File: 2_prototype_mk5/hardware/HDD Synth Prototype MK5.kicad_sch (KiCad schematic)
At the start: 11 parts, among them U2 Optocoupler_DC_PhotoNPN_AKEC

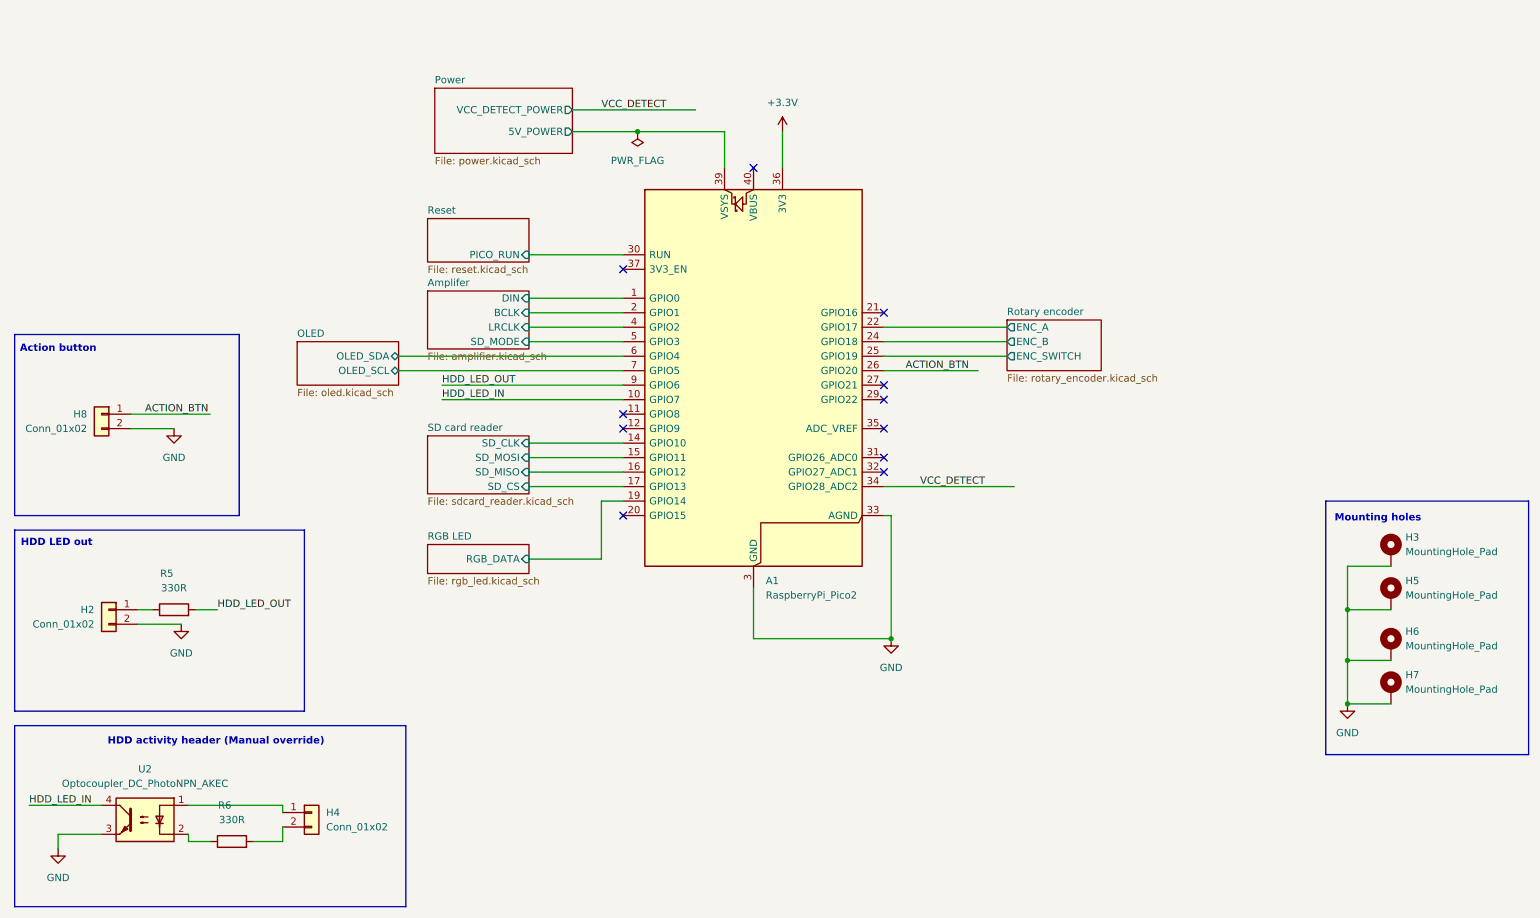
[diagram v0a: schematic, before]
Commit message: MKV - SATA connector and wiring complete
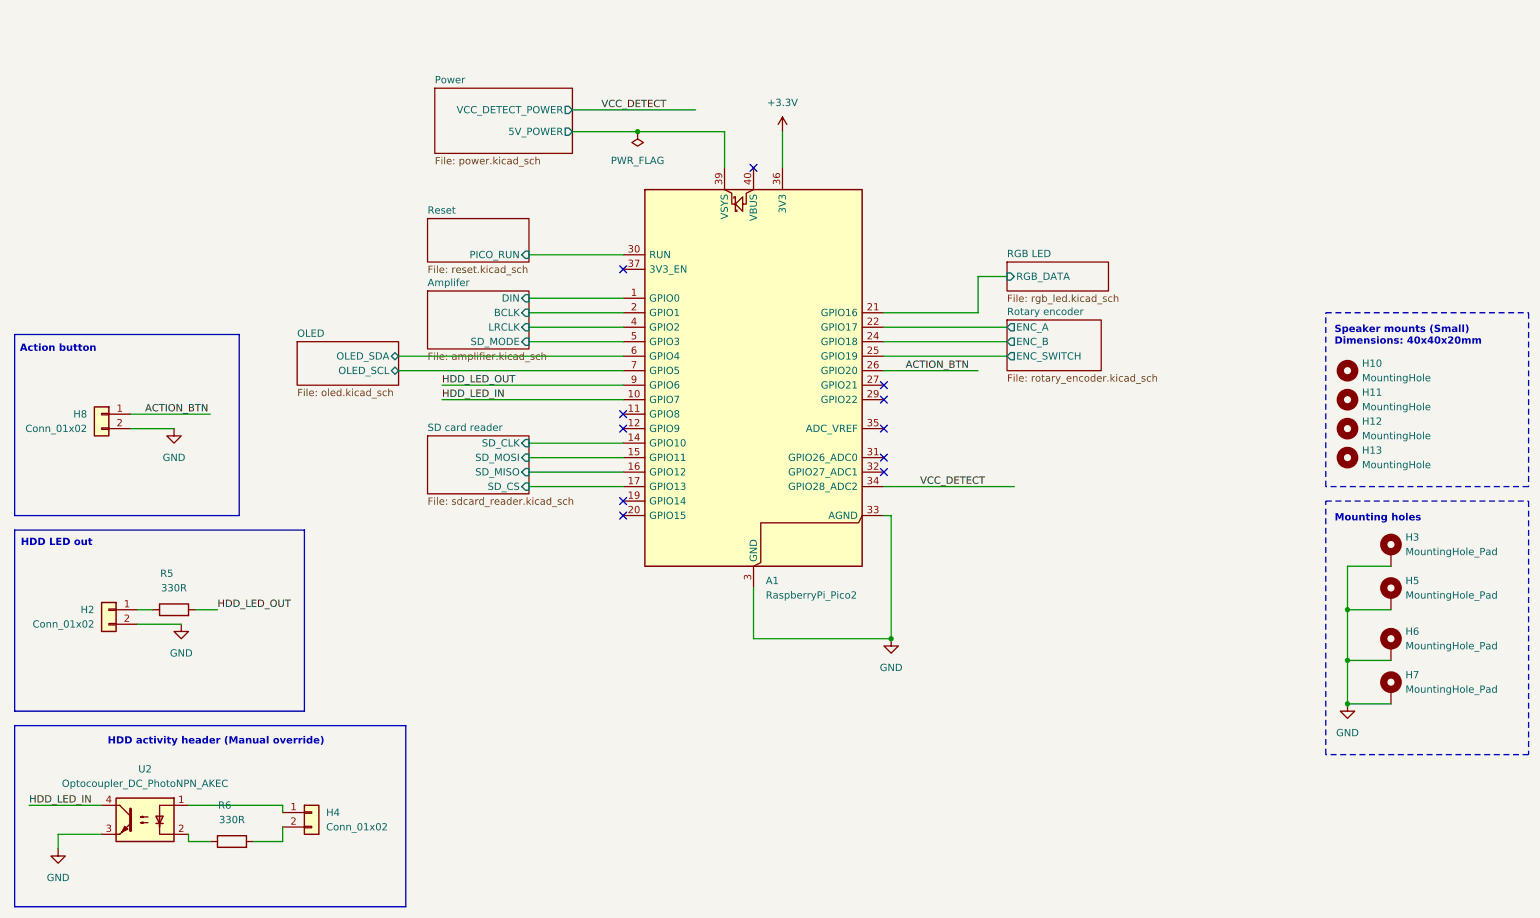
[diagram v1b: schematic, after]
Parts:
- added H10, H11, H12, H13: MountingHole, MountingHole:MountingHole_3.2mm_M3, symbol Mechanical:MountingHole
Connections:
- net RGB LED/RGB_DATA: now also A1.21 (GPIO16); no longer A1.19 (GPIO14)
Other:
- note added: "Speaker mounts (Small) Dimensions: 40x40x20mm"

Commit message: Major MKV redesign using embedded RP2350
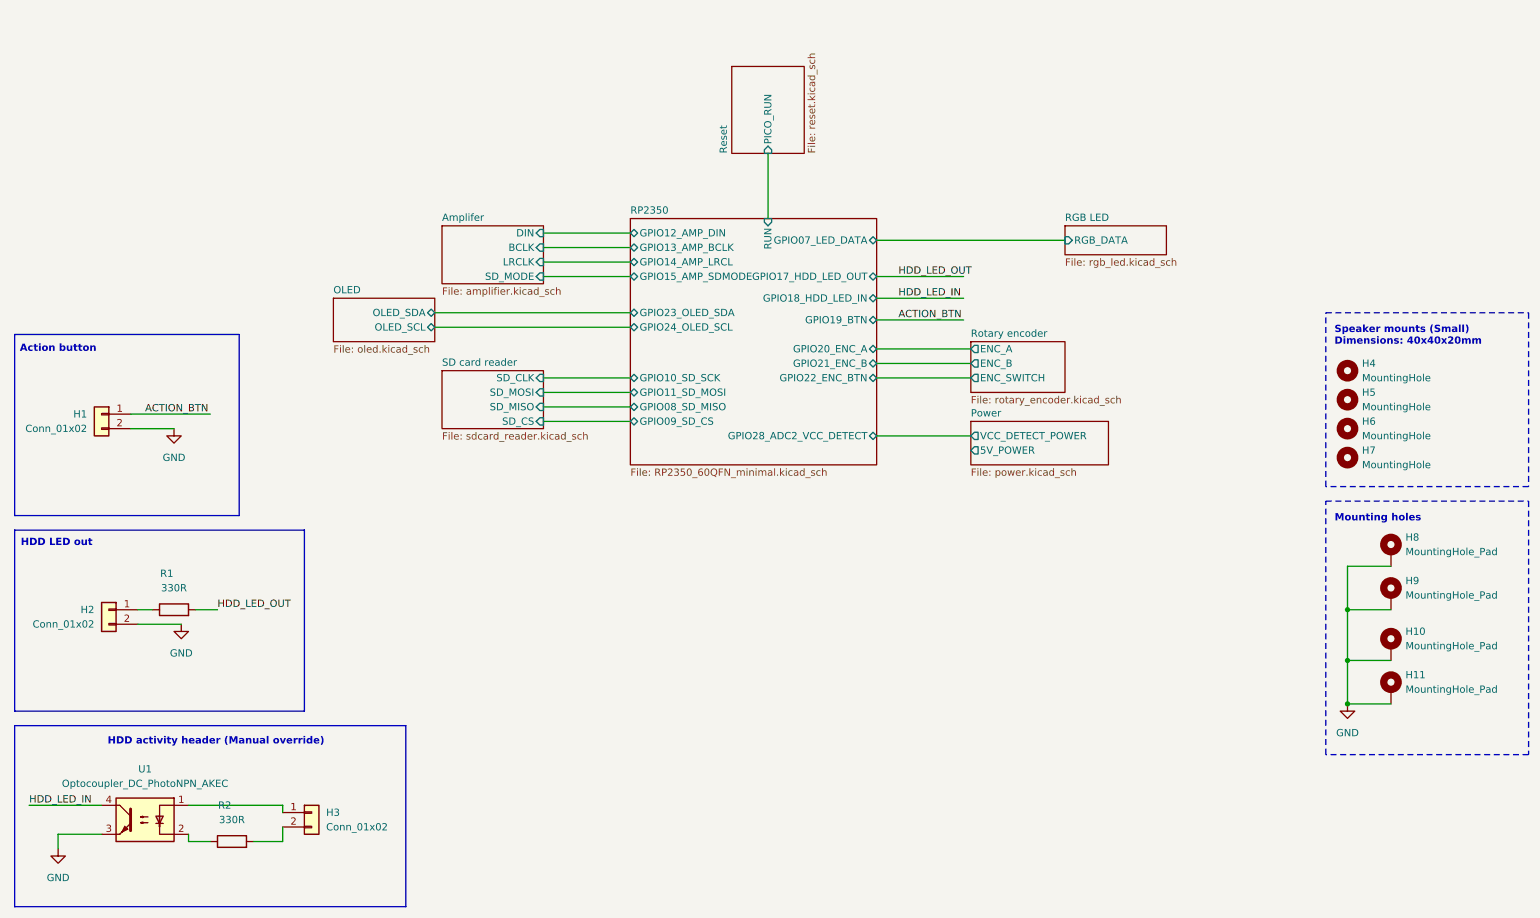
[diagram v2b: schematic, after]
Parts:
- removed A1: RaspberryPi_Pico2, Module:RaspberryPi_Pico_Common_Unspecified, symbol MCU_Module:RaspberryPi_Pico
- renumbered H8 to H1, H6 to H10, H7 to H11, H4 to H3, H10 to H4, H11 to H5, H12 to H6, H13 to H7, H3 to H8, H5 to H9, R5 to R1, R6 to R2, U2 to U1
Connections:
- no-connect marks 11 -> 0
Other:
- added sheet RP2350 (RP2350_60QFN_minimal.kicad_sch)

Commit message: MKV: Add LCSC numbers and resolve DRC errors
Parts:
- H1, H2, H3: LCSC_Part_Number (none) -> C124375
- R1, R2: LCSC_Part_Number (none) -> C23138
